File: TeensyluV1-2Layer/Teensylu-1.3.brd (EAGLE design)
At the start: 101.6 x 76.2 mm, 101 parts, among them J1 M02POLAR, J11 M02POLAR, J12 M02POLAR, J2 MICROSD, J3 USB-MICRO-PTH, J4 M02POLAR, J5 4P-TERM-BLOCK284391-4, J6 39-29-3066, J7 HOTEND-1, J8 2x7, J9 HOTBED, P1 POLOLU-X, P2 POLOLU-Y, P3 POLOLU-Z, P4 POLOLU-E1, Q1 PMV45EN, Q2 PSMN1R2-30YLC, Q3 PSMN1R2-30YLC, Q5 MMUN2211LT3G, U1 LMR16006X, U2 PRTR5V0U4DSOT23-6, U3 AP7313SOT23C, U4 TXB0104TSSOP14, U5 AT90USB1286, X1 16MHZ

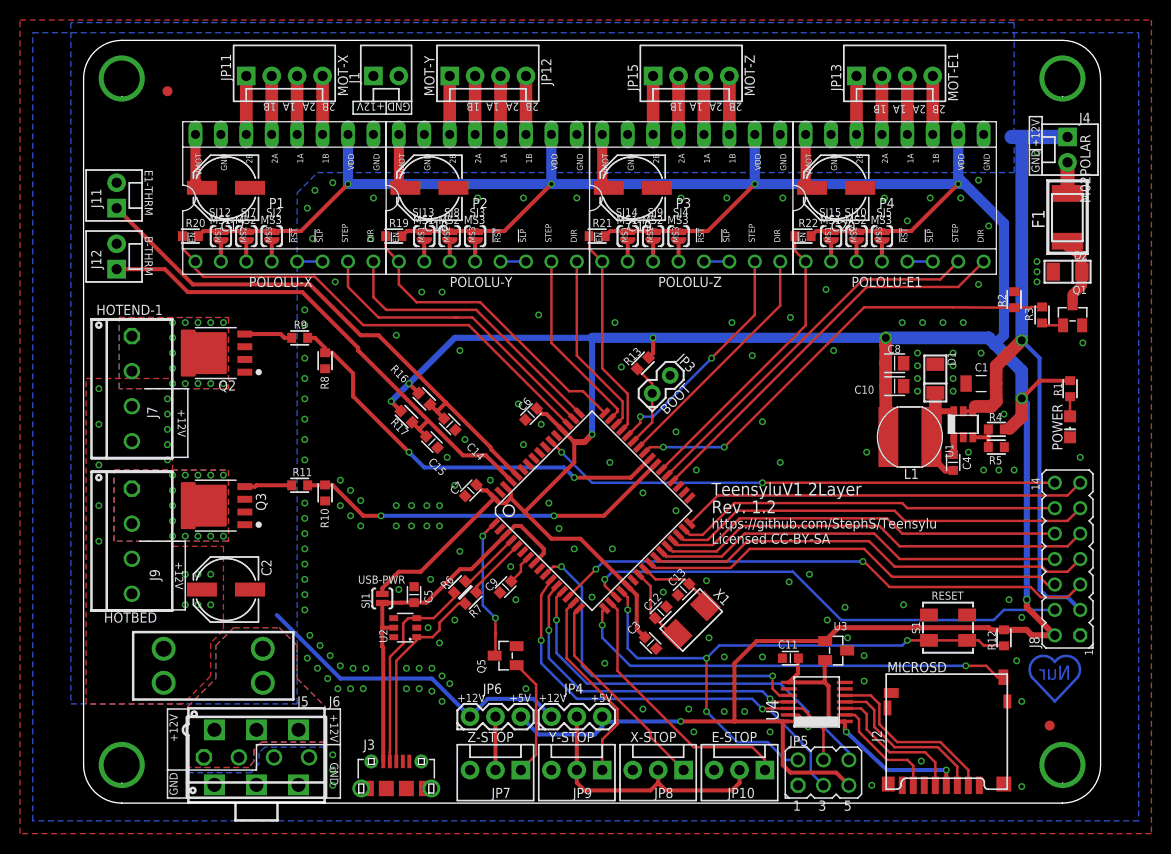
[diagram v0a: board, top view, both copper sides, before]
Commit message: Updated USB Diode, Added Jumper Wires, Z Endstop is now 4 pin
The USB Diode has been changed to DRTR5V0U2SR
22ga jumper wires added to increase current capacity
Z Endstop header is now 4 pin. All future versions will use 4 pin
endstop on Z. See schematics and set the appropriate pinout for your
configuration.
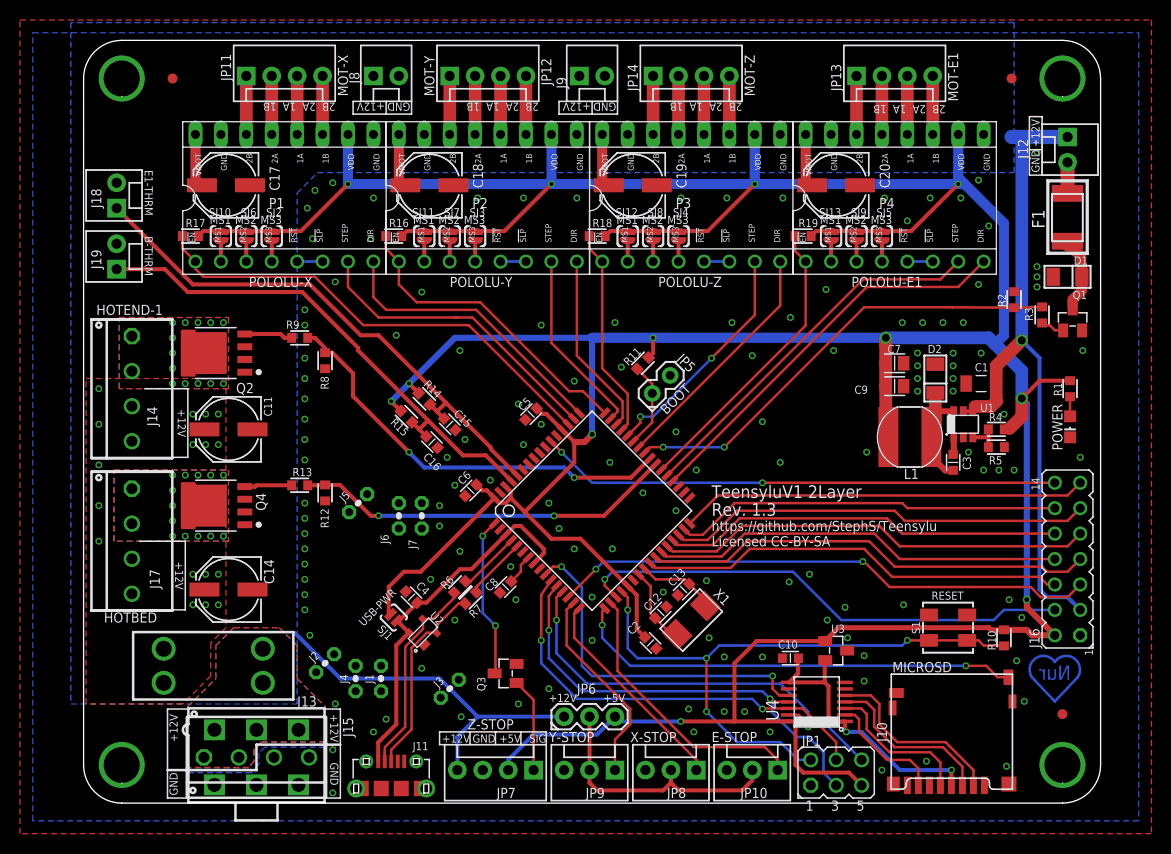
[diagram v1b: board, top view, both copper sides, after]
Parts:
- removed Q5: MMUN2211LT3G, teensylu:SOT23C
- removed R20, R22: 100k, teensylu:RESC1608X55N
- removed SJ14, SJ15: MS1, teensylu:SJ_2S-TRACE
- added C16: 10uF, teensylu:CAPC1608X92N
- added J10: MICROSD, teensylu:AMPHENOL-MICROSD
- added J13: 4P-TERM-BLOCK284391-4, teensylu:284391-4
- added J14: HOTEND-1, teensylu:284391-4
- added J15: 39-29-3066, teensylu:39-29-3066
- added J16: 2x7, teensylu:JP7Q
- added J17: HOTBED, teensylu:284391-4
- added J18, J19: M02POLAR, teensylu:MOLEX-1X2
- added Q4: PSMN1R2-30YLC, teensylu:LFPACK-POWERPAK-SO8
- added R14, R15: 4.7k, teensylu:RESC1608X55N
- added SJ11: MS1, teensylu:SJ_2S-TRACE
- added SJ6: MS2, teensylu:SJ_2S-TRACE
- C10: device teensylu:CAPC2012X145AN -> teensylu:CAPC1608X92N
- C11, C14: value 10uF -> 100uF; device teensylu:CAPC1608X92N -> teensylu:PANASONIC_D
- C2: value 100uF -> 0.1uF; device teensylu:PANASONIC_D -> teensylu:CAPC1608X92N
- C7: value 0.1uF -> 10uF; device teensylu:CAPC1608X92N -> teensylu:CAPC2012X145AN
- C8: value 10uF -> 1uF; device teensylu:CAPC2012X145AN -> teensylu:CAPC1608X92N
- C9: value 1uF -> 10uF; device teensylu:CAPC1608X92N -> teensylu:CAPC2012X145AN
- J1, J4: value M02POLAR -> 22ga; device teensylu:MOLEX-1X2 -> teensylu:WJ_01_08
- J11: value M02POLAR -> USB-MICRO-PTH; device teensylu:MOLEX-1X2 -> teensylu:USB-MICROB-PTH
- J2: value MICROSD -> 22ga; device teensylu:AMPHENOL-MICROSD -> teensylu:WJ_01_08
- J3: value USB-MICRO-PTH -> 22ga; device teensylu:USB-MICROB-PTH -> teensylu:WJ_01_08
- J5: value 4P-TERM-BLOCK284391-4 -> 22ga; device teensylu:284391-4 -> teensylu:WJ_01_08
- J6: value 39-29-3066 -> 22ga; device teensylu:39-29-3066 -> teensylu:WJ_01_08
- J7: value HOTEND-1 -> 22ga; device teensylu:284391-4 -> teensylu:WJ_01_08
- J8: value 2x7 -> M02POLAR; device teensylu:JP7Q -> teensylu:MOLEX-1X2
- J9: value HOTBED -> M02POLAR; device teensylu:284391-4 -> teensylu:MOLEX-1X2
- JP1: value FIDUCIAL1X2.5 -> ISP; device SparkFun:FIDUCIAL-1X2.5 -> teensylu:ISP
- JP3: value BOOT -> FIDUCIAL1X2.5; device teensylu:1X02 -> SparkFun:FIDUCIAL-1X2.5
- JP4: value JUMPER-3PTH -> FIDUCIAL1X2.5; device teensylu:1X03 -> SparkFun:FIDUCIAL-1X2.5
- JP5: value ISP -> BOOT; device teensylu:ISP -> teensylu:1X02
- JP7: value M03POLAR -> Z-STOP; device teensylu:MOLEX-1X3 -> teensylu:MOLEX-1X4
- Q3: value PSMN1R2-30YLC -> MMUN2211LT3G; device teensylu:LFPACK-POWERPAK-SO8 -> teensylu:SOT23C
- R10: value 10k -> 100k
- R11: value 100 -> 100k
- R12: value 100k -> 10k
- R13: value 100k -> 100
- R16, R17: value 4.7k -> 100k
- SJ10: value MS2 -> MS1
- U2: value PRTR5V0U4DSOT23-6 -> DRTR5V0U2SR; device teensylu:SOT23-6 -> teensylu:SOT143-R
- moved JP2 108.9 mm to (8.89, 72.4)
- moved J12 95.9 mm to (98.3, 66.5), turned to 270 degrees
- moved JP1 95.4 mm to (75.2, 3.05)
- moved J4 89.4 mm to (27.2, 12.4), turned to 90 degrees
- moved J8 84.5 mm to (29.0, 72.6), turned to 0 degrees
- moved JP4 78.6 mm to (92.7, 72.4)
- moved R10 69.3 mm to (91.9, 16.5), turned to 90 degrees
- moved R12 69.3 mm to (24.1, 31.0), turned to 270 degrees
- moved J9 64.5 mm to (49.5, 72.6), turned to 0 degrees
- moved J11 64.1 mm to (30.7, 1.46), turned to 0 degrees
- moved SJ10 63.5 mm to (13.7, 56.6)
- moved J2 62.0 mm to (24.1, 14.0), turned to 45 degrees
- moved C11 60.6 mm to (14.5, 37.3)
- moved J1 60.2 mm to (29.7, 12.4), turned to 90 degrees
- moved C4 55.8 mm to (32.8, 20.6), turned to 315 degrees
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- renumbered JP15 to JP14, R21 to R18
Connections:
- removed net Z-STOP-SUPPLY: JP6.2, JP7.2
- net !E1-ENABLE: now also R19.2; no longer R22.2
- net !HOTBED: now also R12.1, R13.1; no longer R10.1, R11.1
- net !RESET: now also JP1.2, R10.1; no longer JP5.2, R12.1
- net !X-ENABLE: now also R17.2; no longer R20.2
- net !Y-ENABLE: now also R16.2; no longer R19.2
- net +3V3: now also C10.1, J10.4; no longer C11.1, J2.4
- net 12V: now also C11.+, C14.+, J12.1, J14.3, J14.4, J16.3, J17.3, J17.4, J8.1, J9.1, JP7.4; no longer C2.+, J1.1, J4.1, J7.3, J7.4, J8.3, J9.3, J9.4, JP4.1
- net 12V_FUSE: now also J13.1, J13.2, J15.1, J15.2, J15.3; no longer J5.1, J5.2, J6.1, J6.2, J6.3
- net 5V: now also C2.1, C5.2, C7.1, C9.1, J16.2, JP1.5, JP7.2, R10.2, R11.2, R14.2, R15.2, R16.1, R17.1, SJ11.2, SJ6.2; no longer C10.1, C3.1, C7.2, C8.1, J8.2, JP4.3, JP5.5, R12.2, R13.2, R16.2, R17.2, R20.1, R22.1, SJ14.2, SJ15.2
- net 5VREG_CB: now also C3.2; no longer C4.2
- net 5VREG_SW: now also C3.1, D2.C; no longer C4.1, D1.C
- net A7: now also J16.14; no longer J8.14
- net ALE: now also JP5.1, R11.1; no longer JP3.1, R13.1
- net B-THERM: now also C16.2, J19.1, R15.1; no longer C15.2, J12.1, R17.1
- net E-MS1: now also SJ13.1; no longer SJ15.1
- net E-MS2: now also SJ9.1; no longer SJ10.1
- net E1-THERM: now also C15.2, J18.1, R14.1; no longer C14.2, J11.1, R16.1
- net ENDSTOP+V: now also JP6.2; no longer JP4.2
- net GND: now also C11.-, C14.-, C16.1, C2.2, C4.1, C7.2, C8.1, C9.2, J1.1, J10.6, J10.C1, J10.C2, J10.C3, J10.C4, J10.CD1, J11.GND, J11.GND1, J11.GND2, J11.GND3, J11.GND4, J11.GND5, J11.GND6, J11.GND7, J11.GND8, J13.3, J13.4, J15.4, J15.5, J15.6, J16.1, J18.2, J19.2, J2.1, J2.2, J3.1, J3.2, J4.1, J4.2, J5.1, J5.2, J6.1, J6.2, J7.1, J7.2, J8.2, J9.2, JP1.1, JP5.2, Q4.1, Q4.2, Q4.3, R12.2, U2.1; no longer C11.2, C14.1, C2.-, C3.2, C7.1, C8.2, C9.1, J11.2, J12.2, J2.6, J2.C1, J2.C2, J2.C3, J2.C4, J2.CD1, J3.GND, J3.GND1, J3.GND2, J3.GND3, J3.GND4, J3.GND5, J3.GND6, J3.GND7, J3.GND8, J5.3, J5.4, J6.4, J6.5, J6.6, J8.1, JP3.2, JP5.1, Q3.1, Q3.3, Q5.2, R10.2, U2.2
- net HOTBED-GND: now also J17.1, J17.2, Q4.5-8; no longer J9.1, J9.2, Q3.5-8
- net HOTEND-GND: now also J14.1, J14.2; no longer J7.1, J7.2
- net MISO: now also JP1.6; no longer JP5.6
- net MOSI: now also JP1.3; no longer JP5.3
- net N$2: now also Q4.4, R13.2; no longer Q3.4, R11.2
- net N$5: now also J12.2; no longer J4.2
- net N$6: now also D1.C; no longer D2.C
- net PB4: now also J16.5; no longer J8.5
- net PD0-SCL: now also J16.6; no longer J8.6
- net PD1-SDA: now also J16.7; no longer J8.7
- net PD2-RX1: now also J16.8; no longer J8.8
- net PD3-TX1: now also J16.9; no longer J8.9
- net PD4: now also J16.10; no longer J8.10
- net PD5: now also J16.11; no longer J8.11
- net PD6: now also J16.12; no longer J8.12
- net PD7: now also J16.13; no longer J8.13
- net PE5: now also J16.4; no longer J8.4
- net SCLK: now also JP1.4; no longer JP5.4
- net SDCD: now also J10.CD2; no longer J2.CD2
- net SDCLK: now also J10.5; no longer J2.5
- net SDCSH: now also J10.2; no longer J2.2
- net SDDI: now also J10.3; no longer J2.3
- net SDDO: now also J10.7; no longer J2.7
- net UCAP: now also C8.2; no longer C9.2
- net USB_DN: now also J11.D-; no longer J3.D-
- net USB_DP: now also J11.D+, U2.2; no longer J3.D+, U2.1
- net VBUS: now also C4.2, J11.VBUS, U2.4; no longer C5.2, J3.VBUS, U2.5
- net X-MS1: now also SJ10.1; no longer SJ12.1
- net X-MS2: now also SJ6.1; no longer SJ7.1
- net Y-MS1: now also SJ11.1; no longer SJ13.1
- net Y-MS2: now also SJ7.1; no longer SJ8.1
- net Z-MS1: now also SJ12.1; no longer SJ14.1
- net Z-MS2: now also SJ8.1; no longer SJ9.1
- net Z-STOP: now also Q3.3; no longer Q5.3
- net Z-STOP-BIAS: now also Q3.1; no longer Q5.1
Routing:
- net Z-STOP-SUPPLY: track 5.33 -> 0.00 mm
- net 5V: track 436.4 -> 441.3 mm
- net 12V: track 122.9 -> 125.8 mm, vias 17 -> 18
- net Z-STOP-BIAS: track 11.9 -> 9.40 mm
- net VBUS: track 39.1 -> 37.2 mm
- net Z-STOP: track 14.3 -> 16.0 mm
- net !RESET: track 61.4 -> 62.6 mm
- net E-STOP: track 26.5 -> 27.8 mm
- net MOSI: track 44.1 -> 45.3 mm
- net MISO: track 44.0 -> 44.8 mm
- net USB_DN: track 21.0 -> 20.4 mm
- net +3V3: track 28.5 -> 29.1 mm
- net SCLK: track 42.6 -> 43.2 mm
- net Y-STOP: track 19.7 -> 20.3 mm
- net X-STOP: track 20.9 -> 21.4 mm
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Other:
- board text added: "Rev. 1.3"
- board text added: "SIG"
- board text removed: "Rev. 1.2"
